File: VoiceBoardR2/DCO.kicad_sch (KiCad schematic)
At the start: 70 parts, among them Q201 BC857, Q202 BC857, U201 TL074, U202 TL074, U203 MCP4451-104E-ST, U204 TL074, U205 MCP4451-104E-ST, U206 TL072

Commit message: new saw to tri converter
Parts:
- added R227, R234: 68k, symbol Device:R_US
- added R235, R236: 10k, PCM_Resistor_SMD_AKL:R_0805_2012Metric, symbol Device:R_US
- R207, R216: value 220k -> 100k
- R223, R226: value 100k -> 39k
- R224, R225: value 220k -> 92k
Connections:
- net SAW1_FULL: now also R234.2; no longer C203.2
- net SAW2_FULL: now also R227.2; no longer C210.2
- net TRI1_FULL: now also C205.2, R209.1; no longer R210.2, U201.8
- net TRI2_FULL: now also C211.2, R220.1; no longer R222.2, U202.8
- net at R201.1, U201.1, U201.2 (-): now also U201.10 (+); no longer D202.2 (A)
- net at C205.1, D201.1 (K), D202.1 (K)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: now also R210.2, R235.2
- net at D204.2 (A), U202.14: no longer R218.2
- net at C211.1, D203.1 (K), D204.1 (K)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: now also R222.2, R236.2
- net at D201.2 (A), U201.14: no longer R202.2
- net at R217.1, U202.1, U202.2 (-): now also U202.10 (+); no longer D203.2 (A)
- new net: D202.2 (A), U201.8
- new net: R218.2, R236.1
- new net: R202.2, R235.1
- new net: D203.2 (A), U202.8
- new net: C203.2, R234.1
- new net: C210.2, R227.1
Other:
- note added: "Saw to triangle converter"
- note added: "Sawtooth DCO core"
- moved on the sheet: C204, C208, C209, C210, C211, C214, C217, C218, D201, D202, D203, D204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

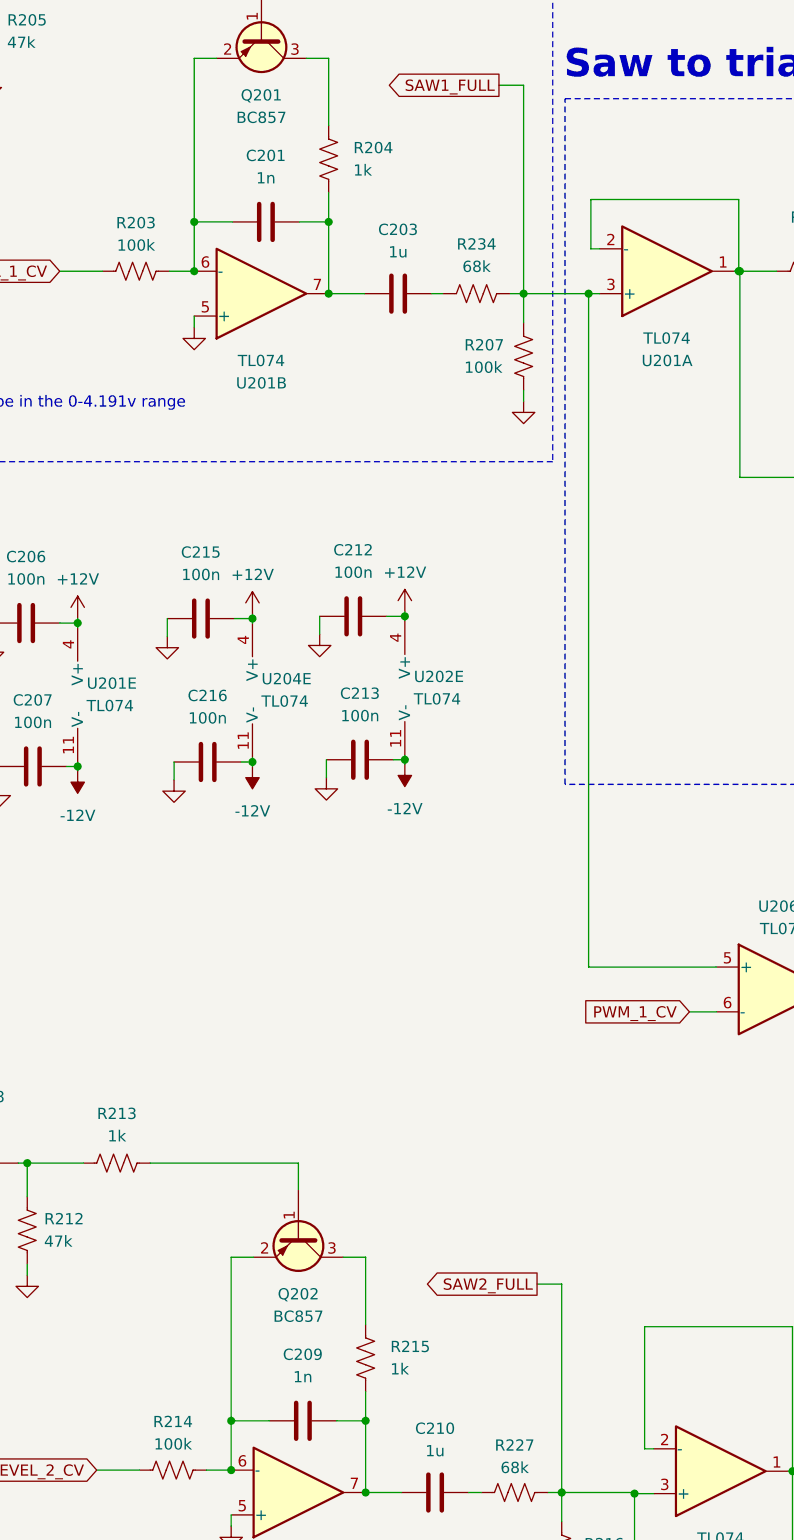
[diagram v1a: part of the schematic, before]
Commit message: op-amp layout improved
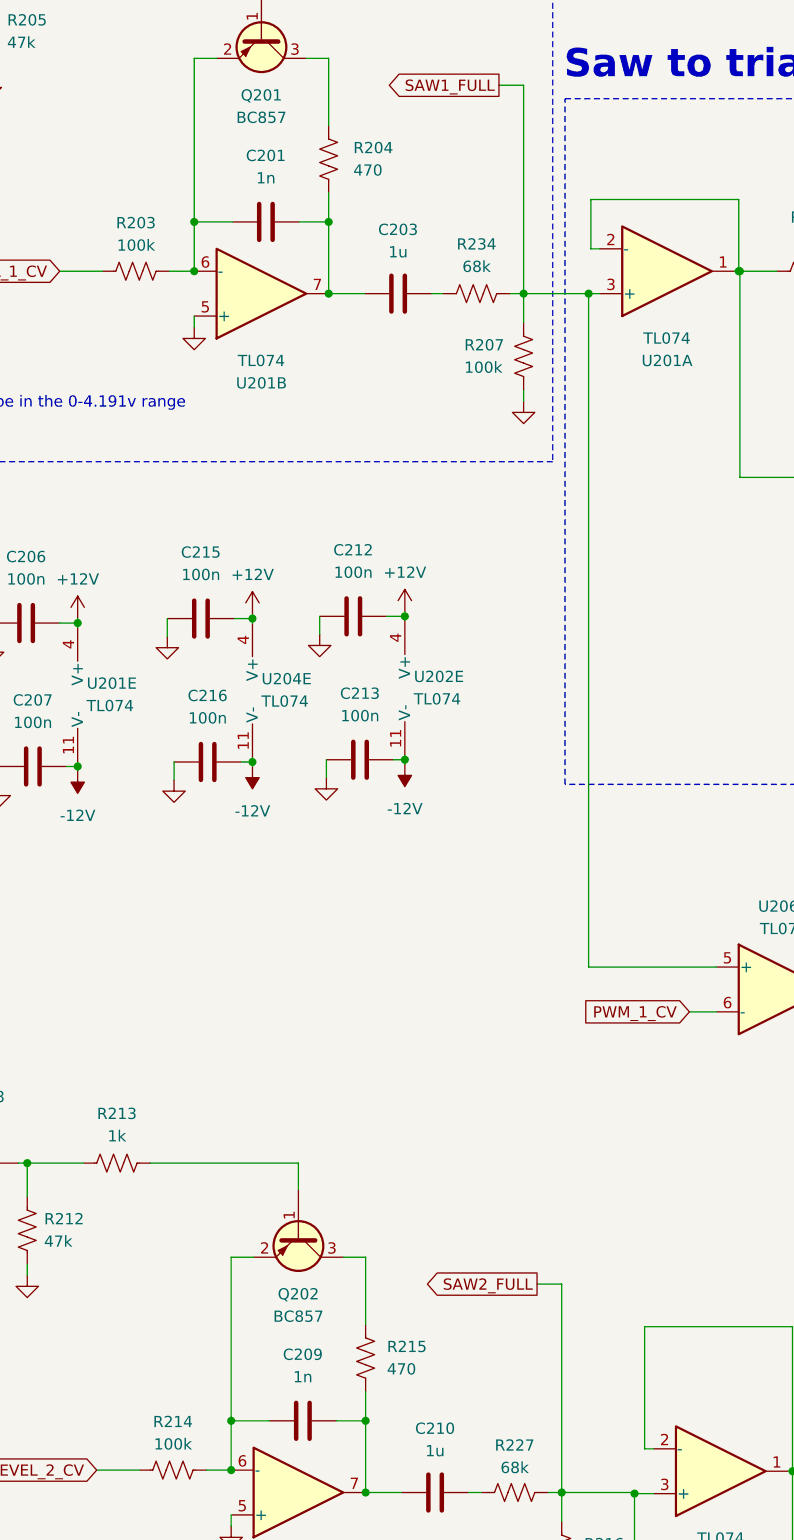
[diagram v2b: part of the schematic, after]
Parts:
- R204, R215: value 1k -> 470
- R227, R234: footprint (none) -> PCM_Resistor_SMD_AKL:R_0805_2012Metric
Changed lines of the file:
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@@
       (effects (font (size 1.27 1.27)) (justify right))
     )
-    (property "Value" "1k" (at 77.47 51.308 0)
+    (property "Value" "470" (at 77.47 51.308 0)
       (effects (font (size 1.27 1.27)) (justify right))
     )
@@
       (effects (font (size 1.27 1.27)))
     )
-    (property "Footprint" "" (at 91.694 64.262 90)
+    (property "Footprint" "PCM_Resistor_SMD_AKL:R_0805_2012Metric" (at 91.694 64.262 90)
       (effects (font (size 1.27 1.27)) hide)
     )
@@
       (effects (font (size 1.27 1.27)))
     )
-    (property "Footprint" "" (at 96.012 200.152 90)
+    (property "Footprint" "PCM_Resistor_SMD_AKL:R_0805_2012Metric" (at 96.012 200.152 90)
       (effects (font (size 1.27 1.27)) hide)
     )
@@
   (symbol (lib_id "Device:R_US") (at 78.867 185.928 180) (unit 1)
     (in_bom yes) (on_board yes) (dnp no) (fields_autoplaced)
-    (property "Reference" "R215" (at 81.661 184.658 0)
+    (property "Reference" "R215" (at 81.28 184.658 0)
       (effects (font (size 1.27 1.27)) (justify right))
     )
-    (property "Value" "1k" (at 81.661 187.198 0)
+    (property "Value" "470" (at 81.28 187.198 0)
       (effects (font (size 1.27 1.27)) (justify right))
     )

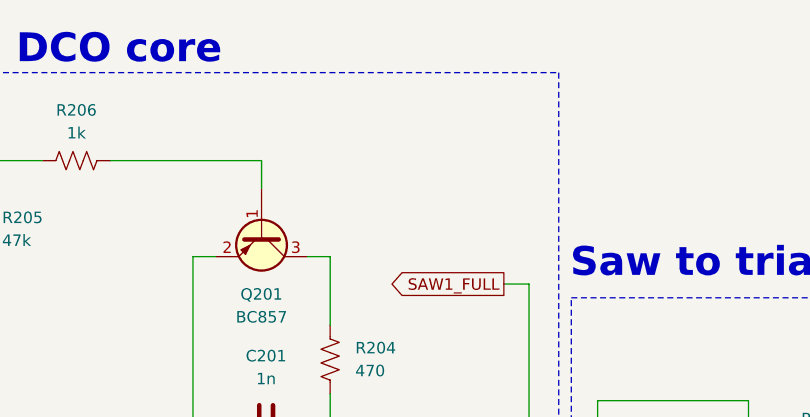
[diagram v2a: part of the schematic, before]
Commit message: footprints placed
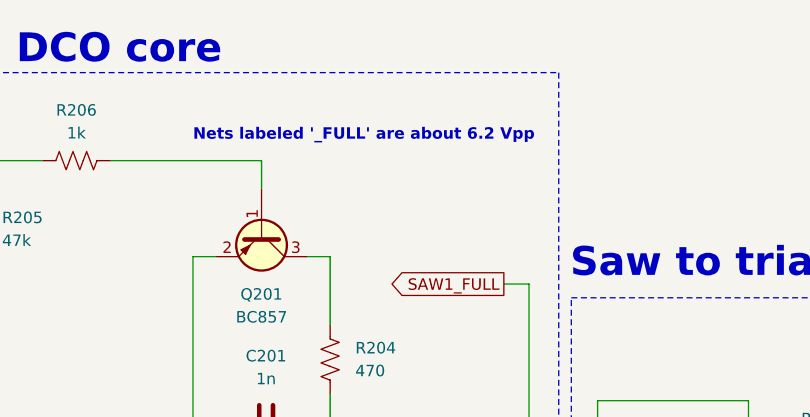
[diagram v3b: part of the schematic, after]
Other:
- note added: "Nets labeled '_FULL' are about 6.2 Vpp"
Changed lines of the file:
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@@
     (effects (font (size 1.27 1.27)) (justify left bottom))
+  )
+  (text "Nets labeled '_FULL' are about 6.2 Vpp" (at 59.436 25.908 0)
+    (effects (font (size 1.27 1.27) (thickness 0.254) bold) (justify left bottom))
   )
   (text "Sawtooth DCO core" (at 14.732 17.526 0)
